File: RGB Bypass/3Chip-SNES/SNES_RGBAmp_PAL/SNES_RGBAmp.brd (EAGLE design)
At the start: 28.4 x 18.6 mm, 22 parts

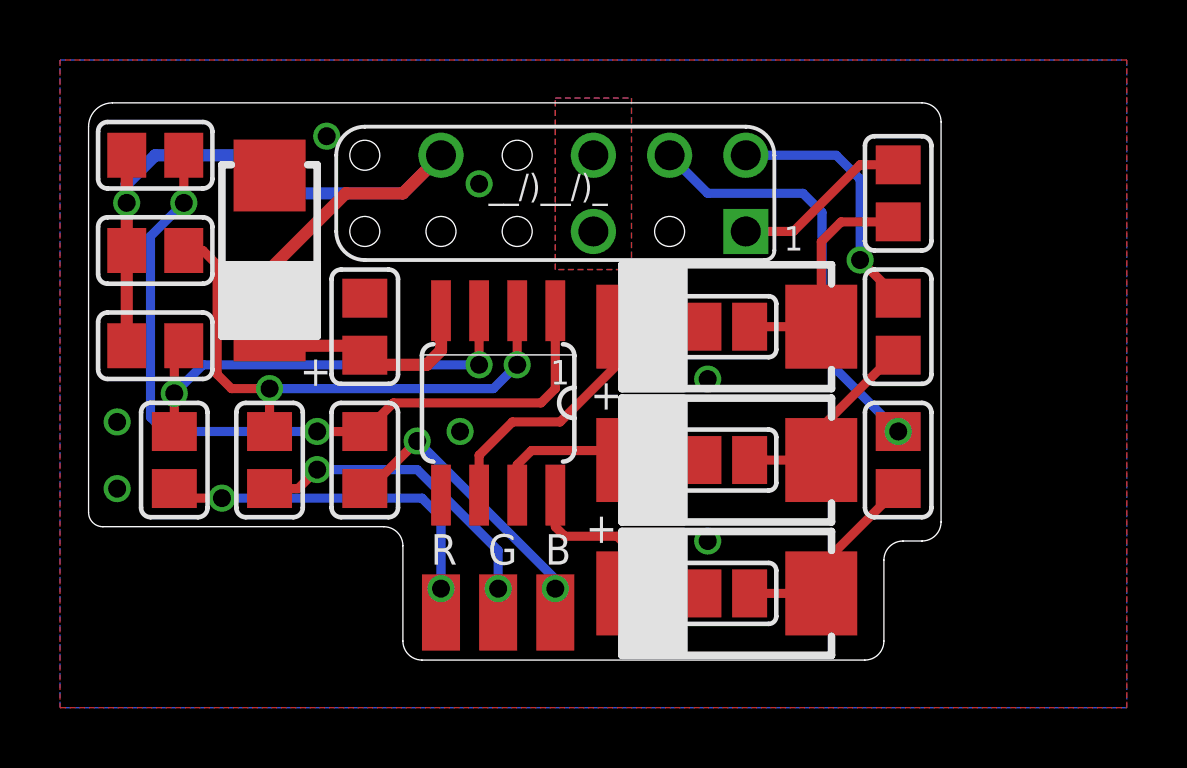
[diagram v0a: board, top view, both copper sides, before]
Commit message: rename folders a bit, add thermals to GND pads
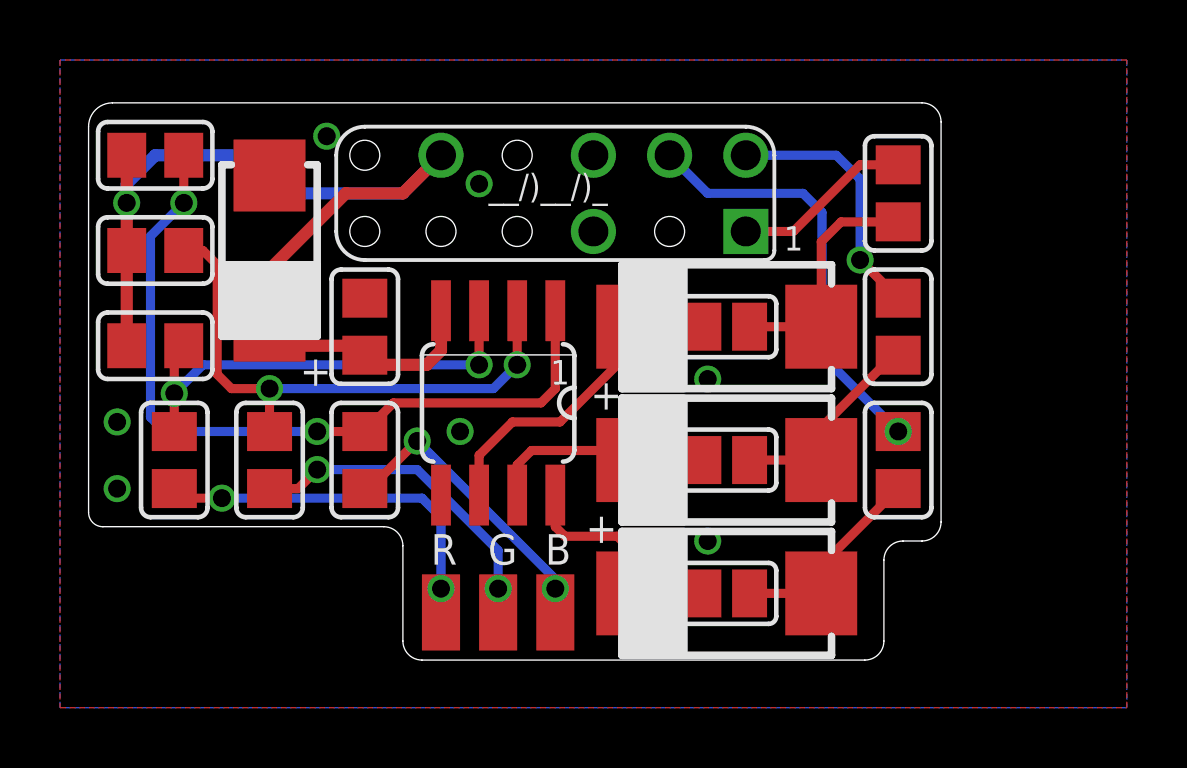
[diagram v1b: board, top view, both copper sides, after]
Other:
- board text added: "PAL- V1.4"
- board text removed: "PAL- V1.2"
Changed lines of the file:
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@@
 <wire x1="12.85875" y1="31.4325" x2="12.85875" y2="28.2575" width="0.1524" layer="22"/>
 <wire x1="12.85875" y1="28.2575" x2="13.17625" y2="27.94" width="0.1524" layer="22" curve="90"/>
-<wire x1="13.97" y1="27.94" x2="14.76375" y2="27.94" width="0.1524" layer="22"/>
+<wire x1="13.17625" y1="27.94" x2="14.76375" y2="27.94" width="0.1524" layer="22"/>
 <wire x1="14.76375" y1="27.94" x2="15.08125" y2="28.2575" width="0.1524" layer="22" curve="90"/>
 <wire x1="15.08125" y1="28.2575" x2="15.08125" y2="28.575" width="0.1524" layer="22"/>
@@
 <wire x1="11.43" y1="34.44875" x2="11.43" y2="32.86125" width="0.1524" layer="22"/>
 <text x="25.4" y="26.51125" size="1.016" layer="22" font="vector" ratio="12" rot="MR0">PAL-
-V1.2</text>
+V1.4</text>
 <wire x1="27.305" y1="33.02" x2="26.9875" y2="33.3375" width="0.1524" layer="22" curve="90"/>
 <wire x1="26.9875" y1="33.3375" x2="22.5425" y2="33.3375" width="0.1524" layer="22"/>
@@
 <vertex x="45.72" y="43.18"/>
 </polygon>
-<polygon width="0.4064" layer="16" thermals="no">
-<vertex x="26.67" y="41.91"/>
-<vertex x="29.21" y="41.91"/>
-<vertex x="29.21" y="36.195"/>
-<vertex x="26.67" y="36.195"/>
-</polygon>
-<polygon width="0.4064" layer="1" thermals="no">
-<vertex x="26.67" y="41.91"/>
-<vertex x="29.21" y="41.91"/>
-<vertex x="29.21" y="36.195"/>
-<vertex x="26.67" y="36.195"/>
-</polygon>
 <via x="31.75" y="27.14625" extent="1-16" drill="0.6"/>
